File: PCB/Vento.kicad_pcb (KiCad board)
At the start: 4 copper layers, 80 x 27 mm, 93 parts, among them J1 B2B-PH-K-S(LF)(SN), J2 B3B-PH-K-S(LF)(SN), J3 20021121-00010C4LF, J4 0475890001-MicroUSBPort, P1 CONN_01X18, P2 CONN_01X18, Q1 DMG2307L-7, Q2 DMG2307L-7, SW1 B3U-1000P, T1 1909763-1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

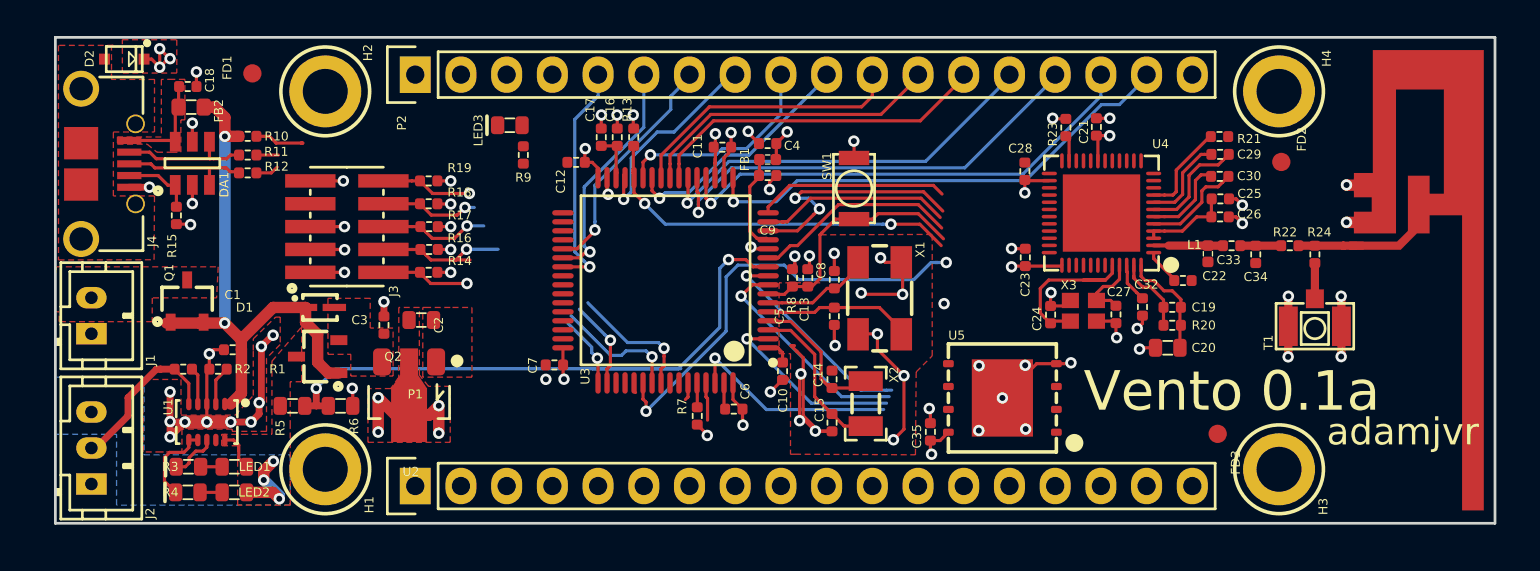
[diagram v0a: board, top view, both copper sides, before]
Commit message: Progress
Headers routed, going to switch SPI flash on ESP32 circuit to SOIC model
for simpler routing.
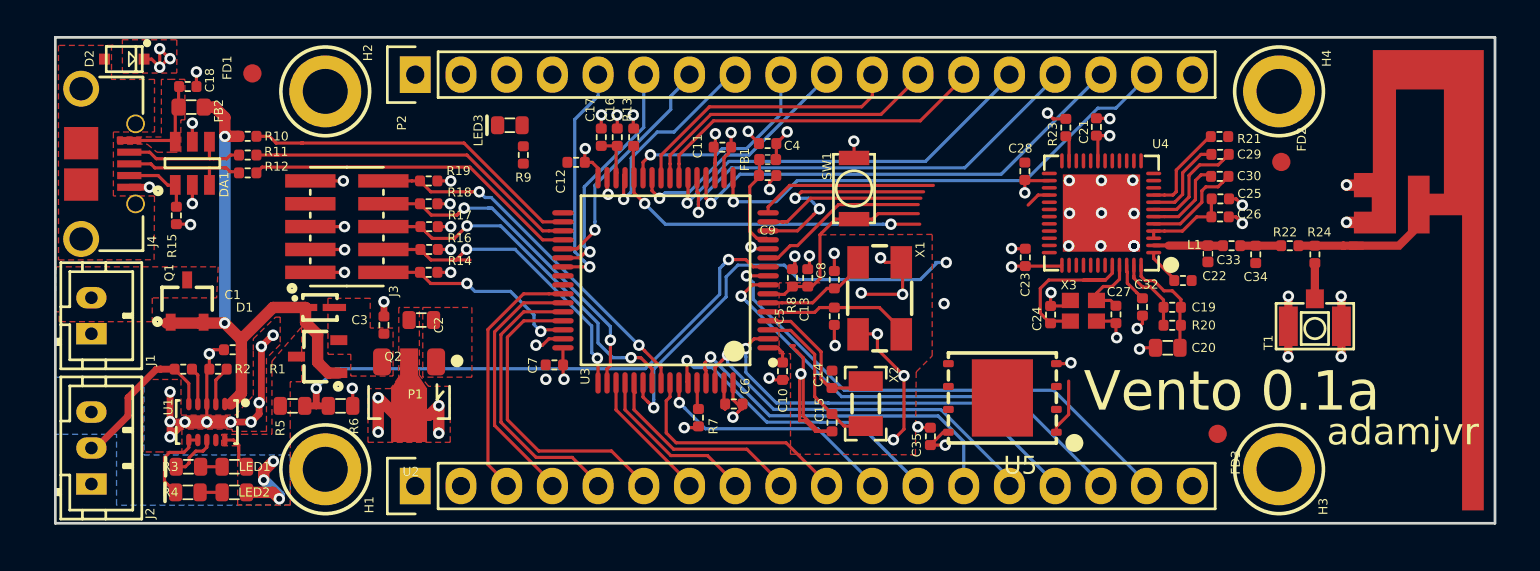
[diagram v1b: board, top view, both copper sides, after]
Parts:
- moved C6 0.29 mm to (183.6, 91.9)
- moved C35 0.25 mm to (194.5, 93.8)
- moved R7 0.12 mm to (181.6, 92.7)
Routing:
- net /MCU_STM32F446RET6/PB8: track 2.10 -> 20.1 mm, vias 0 -> 1
- net Net-(R11-Pad1): track 1.22 -> 18.9 mm
- net Net-(R12-Pad1): track 1.29 -> 18.8 mm
- net /MCU_STM32F446RET6/PA12: track 0.00 -> 17.2 mm
- net /MCU_STM32F446RET6/PC1: track 11.9 -> 28.9 mm
- net Net-(R10-Pad1): track 2.82 -> 19.1 mm
- net /MCU_STM32F446RET6/PB7: track 0.98 -> 17.1 mm, vias 0 -> 1
- net /MCU_STM32F446RET6/PA11: track 0.00 -> 15.8 mm
- net /MCU_STM32F446RET6/PA10: track 0.00 -> 14.4 mm
- net /MCU_STM32F446RET6/PA9: track 0.00 -> 14.1 mm
- net /MCU_STM32F446RET6/PB6: track 0.15 -> 14.1 mm, vias 0 -> 1
- net /MCU_STM32F446RET6/PC0: track 12.3 -> 26.2 mm
- net GND: track 108.9 -> 122.2 mm, vias 67 -> 71
- net /MCU_STM32F446RET6/PB5: track 0.15 -> 13.2 mm
- net /MCU_STM32F446RET6/PC13: track 10.4 -> 22.7 mm
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
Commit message: PCB
PCB done
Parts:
- removed C26: CL05B104JP5NNNC, PCB_Footprints:C0402
- C23, C25: value CL05B104JP5NNNC -> CL10A106KQ8NNNC; footprint PCB_Footprints:C0402 -> PCB_Footprints:C0603
- U5: value W25Q64FVZPIG -> W25Q64FWSSIG; footprint PCB_Footprints:W25Q64FVZPIG -> PCB_Footprints:W25Q64FWSSIG
- moved C35 16.3 mm to (194.4, 77.5)
- moved U5 10.1 mm to (197.4, 81.5), turned to 90 degrees
- moved FD2 6.68 mm to (207.8, 76.1)
- moved C23 3.13 mm to (200.9, 86.7), turned to 180 degrees
- moved FD3 2.82 mm to (207.6, 93.7)
- moved X3 1.97 mm to (204.4, 88.1)
- moved C24 1.97 mm to (202.6, 88.4)
- moved C27 1.97 mm to (206.2, 88.3)
- moved C32 1.66 mm to (207.6, 87.5)
- moved LED3 1.37 mm to (171.9, 77.6)
- moved R9 1.37 mm to (172.6, 79.3)
- moved C28 1.28 mm to (200.3, 77.9)
- moved C19 1.20 mm to (209.1, 87.0)
- moved C20 1.20 mm to (208.8, 89.2)
- moved R20 1.20 mm to (209.1, 88.0)
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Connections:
- U4 pad 24: /MCU_STM32F446RET6/ESPTOST_BOOT0 -> Net-(U4-Pad24)
- U4 pad 25: /MCU_STM32F446RET6/ESPTOST_BOOT1 -> Net-(U4-Pad25)
- U4 pad 35: Net-(U4-Pad35) -> /MCU_STM32F446RET6/ESPTOST_BOOT1
- U4 pad 36: Net-(U4-Pad36) -> /MCU_STM32F446RET6/ESPTOST_BOOT0
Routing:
- net GND: track 122.2 -> 213.9 mm, vias 71 -> 105
- net /MCU_STM32F446RET6/STM_ESP_RST: track 15.2 -> 32.8 mm, vias 0 -> 2
- net /MCU_STM32F446RET6/ESP_PGM_MODE: track 11.0 -> 27.9 mm, vias 0 -> 2
- net /MCU_STM32F446RET6/PA8: track 0.00 -> 16.0 mm, vias 0 -> 1
- net /MCU_STM32F446RET6/PC9: track 0.00 -> 15.2 mm, vias 0 -> 1
- net /MCU_STM32F446RET6/ESP_UTX: track 9.15 -> 20.5 mm, vias 0 -> 2
- net /MCU_STM32F446RET6/ESPTOST_BOOT1: track 19.0 -> 28.8 mm
- net /MCU_STM32F446RET6/ESP_URX: track 12.2 -> 21.9 mm
- net /MCU_STM32F446RET6/ESP_ST_RST: track 11.5 -> 20.6 mm, vias 0 -> 2
- net /WiFi_BLE_ESP32/SD1: track 0.00 -> 8.78 mm, vias 0 -> 2
- net /WiFi_BLE_ESP32/CLK: track 0.00 -> 8.07 mm, vias 0 -> 2
- net /MCU_STM32F446RET6/ESPTOST_BOOT0: track 23.9 -> 31.9 mm
- net /WiFi_BLE_ESP32/SD3: track 0.00 -> 7.72 mm, vias 0 -> 2
- net +3V3: track 46.3 -> 53.3 mm, vias 22 -> 24
- net /WiFi_BLE_ESP32/SDO: track 0.00 -> 6.68 mm
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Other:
- net class Default: clearance 0.1778 -> 0.1524
- rule trace_clearance: 0.1778 -> 0.1524
- rule trace_min: 0.1778 -> 0.1524

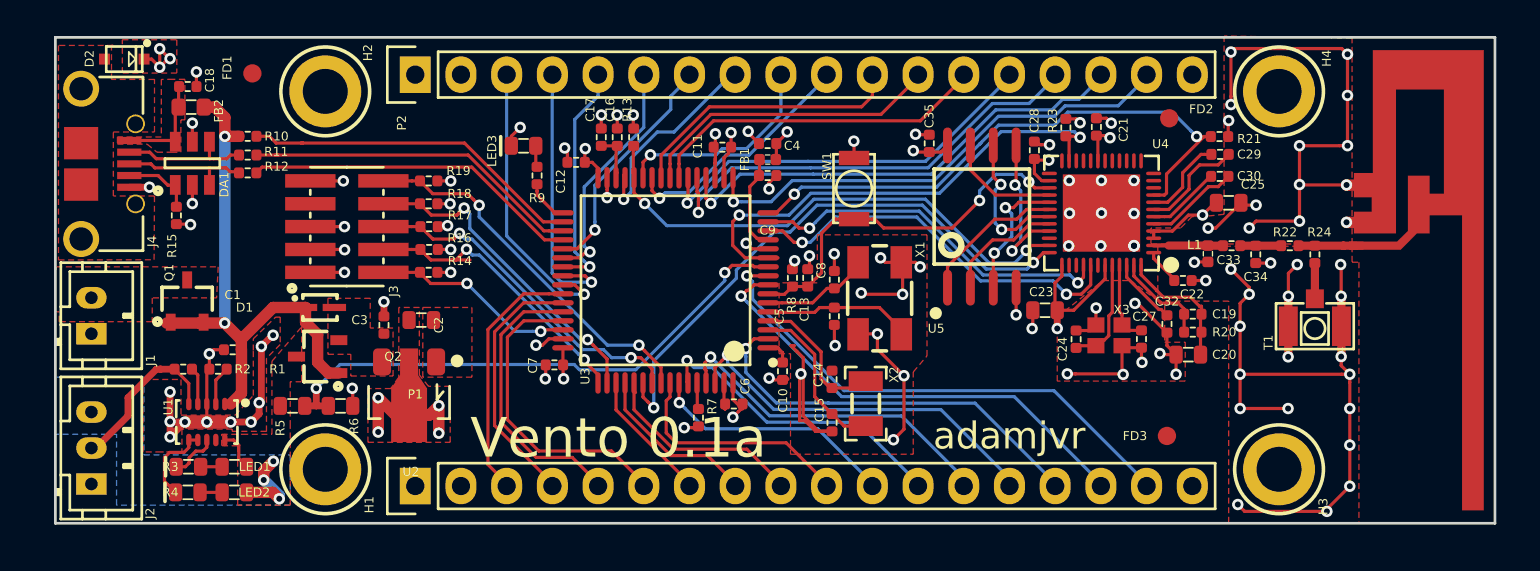
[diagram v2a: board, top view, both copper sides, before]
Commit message: Tweaking and ESP3212 version
Continuing to tweak the PCB, for optimal RF performance, thinking about
capping either the RF section of the MCU+RF entirely. Also made an
ESP3212 module version, both will be built at the same time when the
time comes.
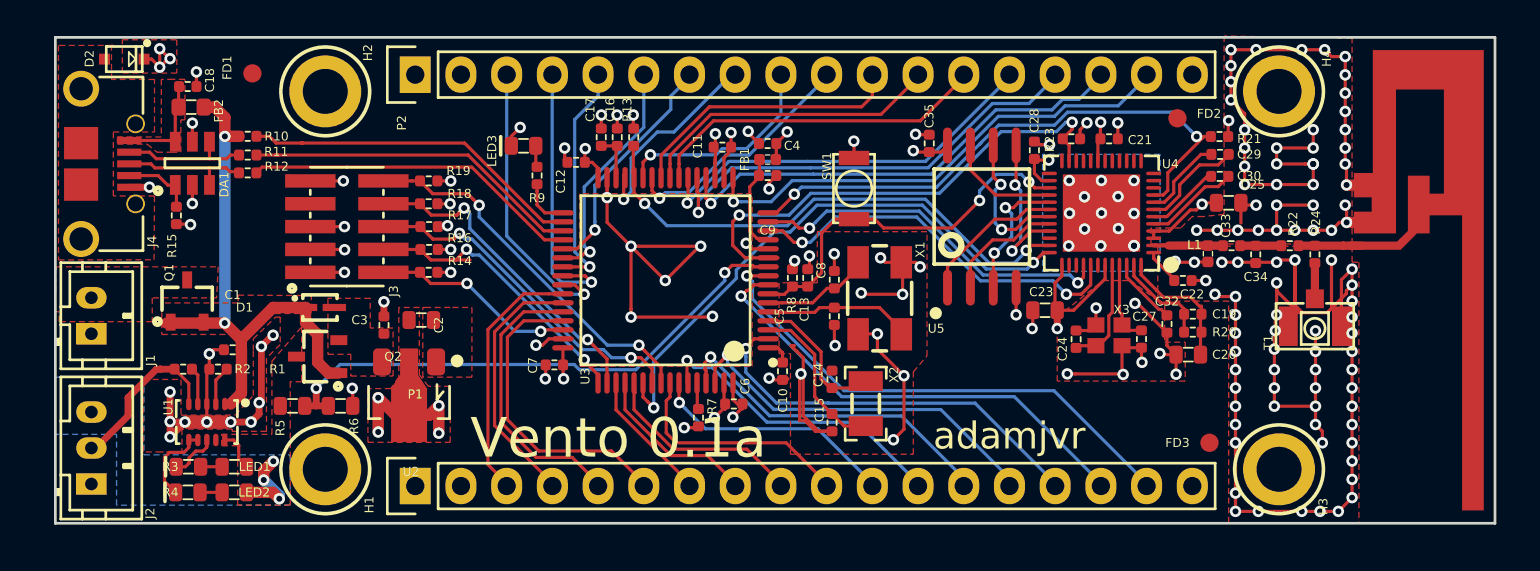
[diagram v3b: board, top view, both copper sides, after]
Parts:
- moved FD3 2.39 mm to (210.0, 94.1)
- moved C21 0.97 mm to (204.4, 77.2), turned to 0 degrees
- moved R23 0.70 mm to (202.3, 77.2), turned to 180 degrees
- moved FD2 0.46 mm to (208.2, 76.1)
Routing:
- net GND: track 213.9 -> 290.6 mm, vias 105 -> 173
- added copper zone on F.Cu, net /MCU_STM32F446RET6/VBUS
- added copper zone on B.Cu, net GND

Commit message: Tweaks, DRC cleared, images, readme
Tweaked both designs according to the dev board scheamtics provided by
Espressif in the datasheets folder. Cleared both boards of DRC
violations, added new images and updated the readme.
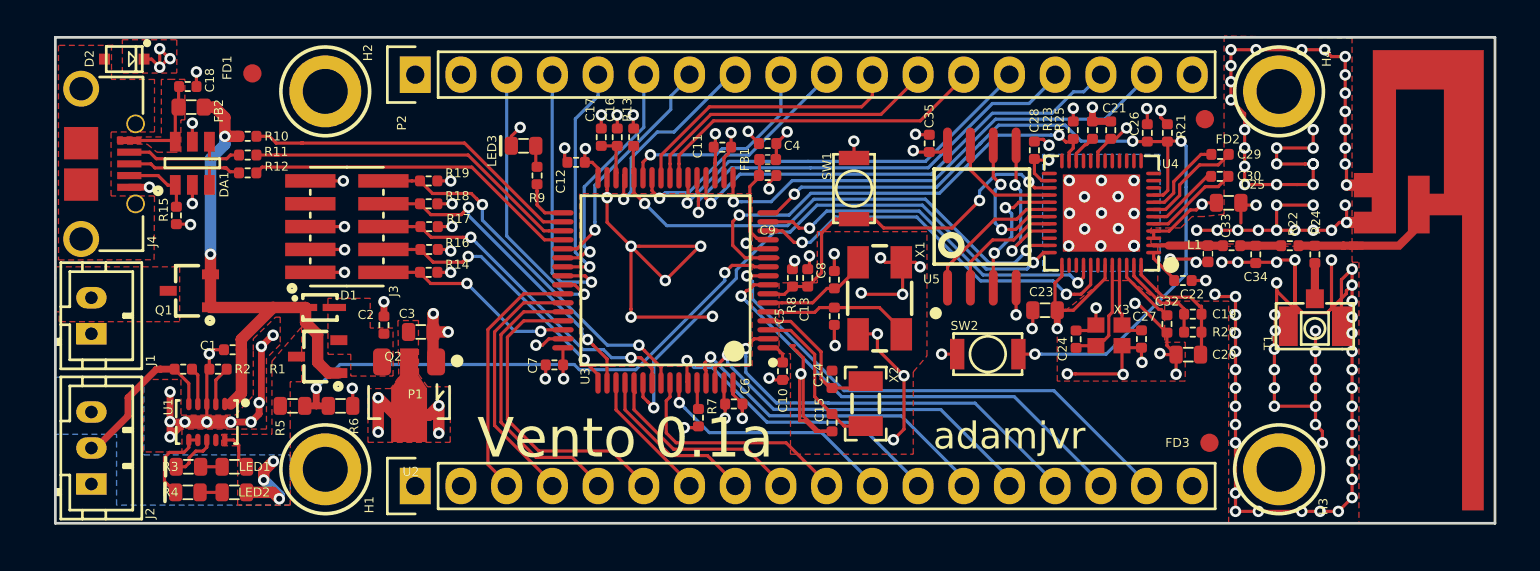
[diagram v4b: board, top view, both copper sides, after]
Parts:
- added C26: CL05B104JP5NNNC, PCB_Footprints:C0402, F.Cu at (206.6, 76.9)
- added R25: RC1005F103CS, PCB_Footprints:R0402, F.Cu at (203.5, 76.7)
- added SW2: B3U-1000P, PCB_Footprints:B3U-1000P, F.Cu at (197.7, 89.2)
- moved R21 2.90 mm to (207.7, 76.9), turned to 270 degrees
- moved FD2 1.52 mm to (209.8, 76.1)
- moved C3 0.66 mm to (166.2, 87.9)
- moved Q1 0.58 mm to (153.3, 85.7), turned to 180 degrees
- moved R23 0.49 mm to (202.4, 76.7), turned to 270 degrees
- moved C21 0.49 mm to (204.5, 76.7), turned to 90 degrees
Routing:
- net /MCU_STM32F446RET6/STM_ESP_RST: track 32.7 -> 47.8 mm, vias 2 -> 4
- net GND: track 290.6 -> 297.1 mm, vias 173 -> 177
- net /MCU_STM32F446RET6/VBUS: track 31.4 -> 29.6 mm
- net Net-(R25-Pad2): track 0.00 -> 1.64 mm
- net /MCU_STM32F446RET6/SWCLK_TCK: track 16.8 -> 15.6 mm
- net /MCU_STM32F446RET6/ESP_PGM_MODE: track 27.8 -> 26.7 mm
- net +3V3: track 53.5 -> 54.5 mm
- removed copper zone on F.Cu, net /MCU_STM32F446RET6/VBUS

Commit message: On/Off And Cleanup
Onoff Switch added, PCB extended 1mm to accomodated everything. routing
and traes cleaned up. Heat sinking ground pours added to the BQ chip
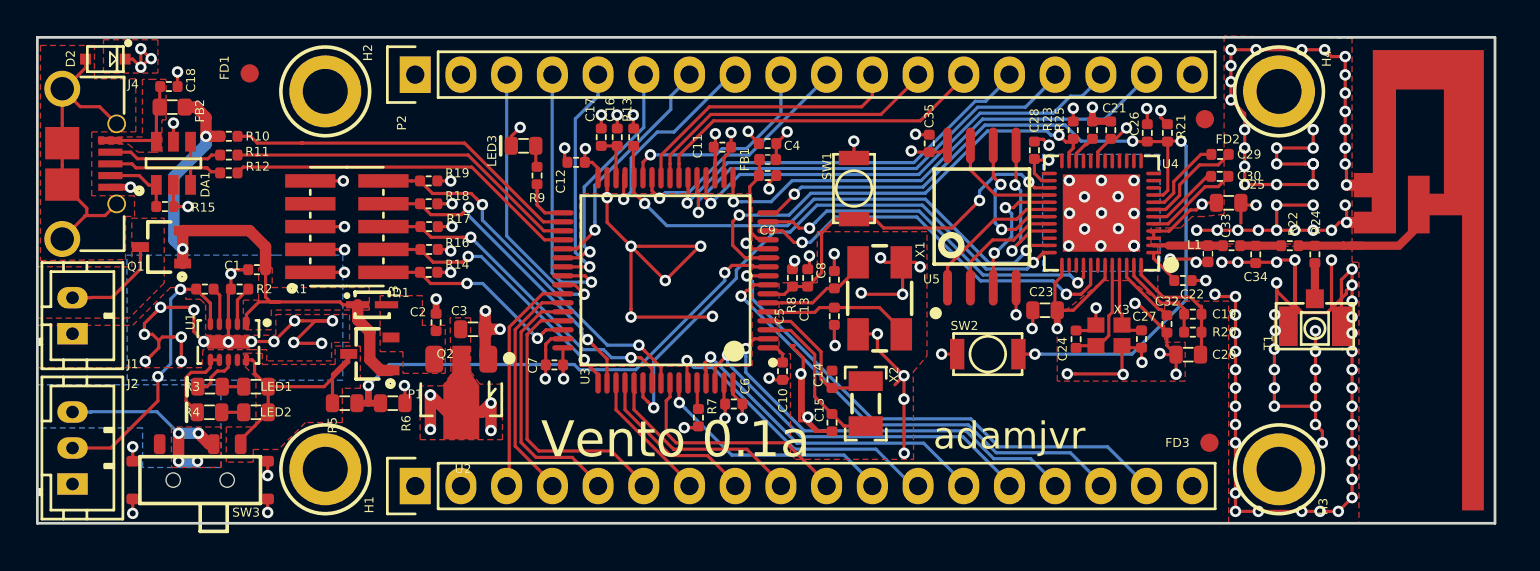
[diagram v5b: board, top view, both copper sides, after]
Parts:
- added SW3: CUS-12TB, PCB_Footprints:CUS-12TB, F.Cu at (153.9, 96.2)
- moved C1 4.65 mm to (157.1, 84.5)
- moved LED1 4.61 mm to (154.5, 91.0)
- moved R3 4.61 mm to (157.0, 91.0)
- moved R4 4.61 mm to (157.0, 92.4)
- moved LED2 4.61 mm to (154.4, 92.4)
- moved R2 4.61 mm to (154.2, 85.6)
- moved U1 4.61 mm to (155.5, 88.6)
- moved R1 4.61 mm to (156.1, 85.6)
- moved C3 2.90 mm to (169.1, 87.8)
- moved D1 2.90 mm to (163.5, 86.4)
- moved R5 2.90 mm to (162.0, 91.9)
- moved R6 2.90 mm to (164.6, 91.9)
- moved C2 2.90 mm to (167.0, 87.4)
- moved Q2 2.90 mm to (163.4, 89.2)
- moved U2 2.90 mm to (168.4, 91.3)
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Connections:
- J2 pad 3: /Power/BAT -> Net-(J2-Pad3)
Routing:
- net GND: track 297.1 -> 315.0 mm, vias 177 -> 185
- net Net-(D2-Pad1): track 0.00 -> 17.6 mm
- net Net-(J2-Pad3): track 0.00 -> 11.2 mm, vias 0 -> 4
- net /Power/BAT: track 6.90 -> 14.6 mm, vias 3 -> 0
- net /Power/THERM: track 9.31 -> 15.7 mm, vias 0 -> 2
- net Net-(J1-Pad2): track 0.00 -> 6.01 mm
- net /MCU_STM32F446RET6/VBUS: track 29.6 -> 33.0 mm
- net /MCU_STM32F446RET6/BAT_VOLT: track 30.8 -> 27.8 mm
- net /MCU_STM32F446RET6/PA10: track 14.4 -> 12.8 mm
- net /MCU_STM32F446RET6/PA11: track 15.8 -> 14.3 mm
- net /MCU_STM32F446RET6/PA9: track 14.1 -> 12.6 mm
- net /MCU_STM32F446RET6/PA12: track 17.2 -> 15.8 mm
- net Net-(R10-Pad1): track 19.1 -> 20.1 mm
- net Net-(R12-Pad1): track 18.8 -> 19.9 mm
- net Net-(R11-Pad1): track 18.9 -> 19.8 mm
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- added copper zone on F.Cu, net /MCU_STM32F446RET6/VBUS
- added copper zone on B.Cu, net Net-(J2-Pad3)
- added copper zone on F.Cu, net Net-(J2-Pad3)
- removed copper zone on B.Cu, net /Power/BAT
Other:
- board size 80 x 27 mm -> 81 x 27 mm
